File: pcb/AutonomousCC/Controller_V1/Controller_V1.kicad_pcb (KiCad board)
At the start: 2 copper layers, 142.9 x 87.6 mm, 18 parts, among them J1 Antenna_Conn_02x04_Odd_Even, J2 USB1130-15-A_REVA, SW1 SW_12mm_Push, SW2 SW_12mm_Push, U1 COM-09032, U2 Pico, U3 COM-09032

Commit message: Updated Tracing
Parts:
- turned VR1 to 270 degrees
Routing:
- net +3V3: track 0.00 -> 216.9 mm, vias 0 -> 2
- net +5V: track 0.00 -> 168.5 mm
- net GP04: track 0.00 -> 71.6 mm, vias 0 -> 1
- net GP27: track 0.00 -> 71.1 mm
- net GP28: track 0.00 -> 65.6 mm
- net GP06: track 0.00 -> 58.8 mm, vias 0 -> 1
- net GP26: track 0.00 -> 52.3 mm
- net GP07: track 0.00 -> 51.4 mm, vias 0 -> 1
- net GP15: track 0.00 -> 41.3 mm
- net GP10: track 0.00 -> 39.2 mm
- net GP16: track 0.00 -> 37.1 mm
- net GP09: track 0.00 -> 32.9 mm
- net GP14: track 0.00 -> 28.6 mm
- net Net-(D1-Pad2): track 0.00 -> 25.2 mm
- net GP17: track 0.00 -> 25.2 mm
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
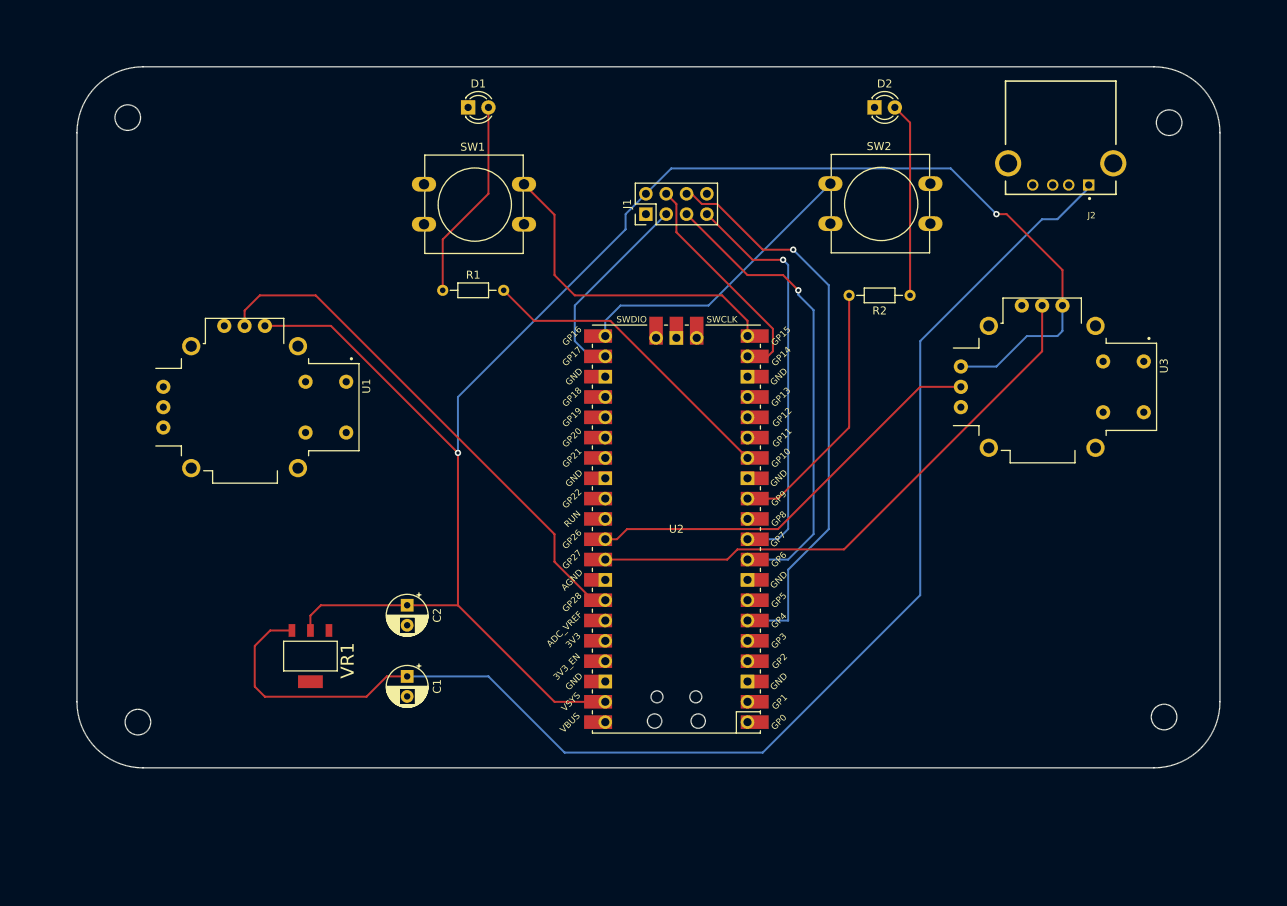
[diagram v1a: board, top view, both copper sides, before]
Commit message: Updated Ground Layer
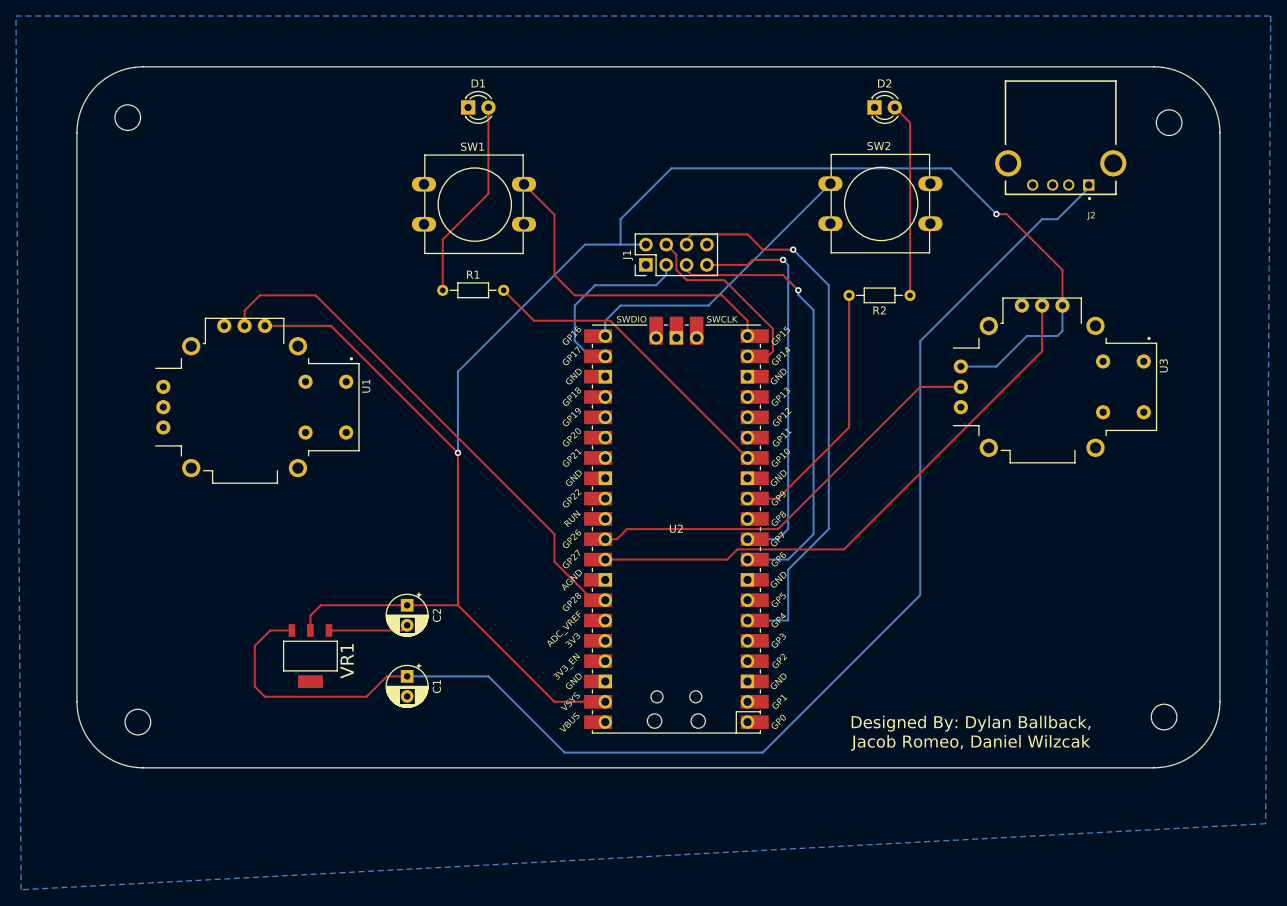
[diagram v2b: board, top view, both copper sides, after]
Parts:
- moved J1 6.35 mm to (170.8, 75.6)
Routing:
- net GND: track 0.00 -> 10.0 mm
- net +3V3: track 216.9 -> 224.0 mm
- net GP14: track 28.6 -> 25.1 mm
- net GP06: track 58.8 -> 56.5 mm
- net GP07: track 51.4 -> 49.3 mm
- net GP17: track 25.2 -> 23.3 mm
- net GP04: track 71.6 -> 70.4 mm
- added copper zone on B.Cu, net GND
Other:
- board text added: "Designed By: Dylan Ballback, Jacob Romeo, Daniel Wilzcak"
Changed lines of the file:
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@@
   (general
     (thickness 1.6)
-    (drawings 8)
-    (tracks 122)
+    (drawings 9)
+    (tracks 133)
     (zones 0)
     (modules 18)
@@
   )
   (module Connector_PinHeader_2.54mm:PinHeader_2x04_P2.54mm_Vertical (layer F.Cu)
-    (at 170.815 69.215 90)
+    (at 170.815 75.565 90)
     (descr "Through hole straight pin header, 2x04, 2.54mm pitch, double rows")
     (tags "Through hole pin header THT 2x04 2.54mm double row")
@@
     )
   )
+  (gr_text "Designed By: Dylan Ballback, \nJacob Romeo, Daniel Wilzcak\n" (at 211.455 133.985) (layer F.SilkS)
+    (effects (font (size 1.5 1.5) (thickness 0.25)))
+  )
   (gr_arc (start 234.315 59.055) (end 242.57 59.055) (angle -90) (layer Edge.Cuts) (width 0.05))
   (gr_arc (start 107.95 59.055) (end 107.95 50.8) (angle -90) (layer Edge.Cuts) (width 0.05))
@@
   (segment (start 187.96 74.93) (end 187.96 74.93) (width 0.25) (layer B.Cu) (net 2))
   (via (at 187.96 74.93) (size 0.8) (drill 0.4) (layers F.Cu B.Cu) (net 2))
-  (segment (start 184.15 74.93) (end 178.435 69.215) (width 0.25) (layer F.Cu) (net 2))
+  (segment (start 183.515 75.565) (end 178.435 75.565) (width 0.25) (layer F.Cu) (net 2))
+  (segment (start 184.15 74.93) (end 183.515 75.565) (width 0.25) (layer F.Cu) (net 2))
   (segment (start 187.96 74.93) (end 184.15 74.93) (width 0.25) (layer F.Cu) (net 2))
   (segment (start 183.515 120.015) (end 188.595 120.015) (width 0.25) (layer B.Cu) (net 3))
@@
   (segment (start 189.23 73.66) (end 189.23 73.66) (width 0.25) (layer B.Cu) (net 3))
   (via (at 189.23 73.66) (size 0.8) (drill 0.4) (layers F.Cu B.Cu) (net 3))
-  (segment (start 176.53 66.675) (end 175.895 66.675) (width 0.25) (layer F.Cu) (net 3))
-  (segment (start 177.8 67.945) (end 176.53 66.675) (width 0.25) (layer F.Cu) (net 3))
-  (segment (start 179.705 67.945) (end 177.8 67.945) (width 0.25) (layer F.Cu) (net 3))
-  (segment (start 185.42 73.66) (end 179.705 67.945) (width 0.25) (layer F.Cu) (net 3))
+  (segment (start 176.53 71.755) (end 175.895 72.39) (width 0.25) (layer F.Cu) (net 3))
+  (segment (start 183.515 71.755) (end 176.53 71.755) (width 0.25) (layer F.Cu) (net 3))
+  (segment (start 185.42 73.66) (end 183.515 71.755) (width 0.25) (layer F.Cu) (net 3))
+  (segment (start 175.895 72.39) (end 175.895 73.025) (width 0.25) (layer F.Cu) (net 3))
   (segment (start 189.23 73.66) (end 185.42 73.66) (width 0.25) (layer F.Cu) (net 3))
   (via (at 189.86501 78.74) (size 0.8) (drill 0.4) (layers F.Cu B.Cu) (net 4))
-  (segment (start 189.865 78.74) (end 189.86501 78.74) (width 0.25) (layer F.Cu) (net 4))
-  (segment (start 187.96 76.835) (end 189.865 78.74) (width 0.25) (layer F.Cu) (net 4))
-  (segment (start 183.515 76.835) (end 187.96 76.835) (width 0.25) (layer F.Cu) (net 4))
-  (segment (start 175.895 69.215) (end 183.515 76.835) (width 0.25) (layer F.Cu) (net 4))
   (segment (start 189.86501 79.305685) (end 189.86501 78.74) (width 0.25) (layer B.Cu) (net 4))
   (segment (start 188.595 112.395) (end 191.77 109.22) (width 0.25) (layer B.Cu) (net 4))
@@
   (segment (start 191.77 109.22) (end 191.77 81.210675) (width 0.25) (layer B.Cu) (net 4))
   (segment (start 183.515 112.395) (end 188.595 112.395) (width 0.25) (layer B.Cu) (net 4))
+  (segment (start 187.96 76.835) (end 189.865 78.74) (width 0.25) (layer F.Cu) (net 4))
+  (segment (start 176.53 76.835) (end 187.96 76.835) (width 0.25) (layer F.Cu) (net 4))
+  (segment (start 189.865 78.74) (end 189.86501 78.74) (width 0.25) (layer F.Cu) (net 4))
+  (segment (start 175.895 76.2) (end 176.53 76.835) (width 0.25) (layer F.Cu) (net 4))
+  (segment (start 175.895 75.565) (end 175.895 76.2) (width 0.25) (layer F.Cu) (net 4))
+  (segment (start 174.625 76.201411) (end 174.625 74.295) (width 0.25) (layer F.Cu) (net 5))
   (segment (start 183.515 86.995) (end 186.055 86.995) (width 0.25) (layer F.Cu) (net 5))
   (segment (start 186.055 86.995) (end 186.69 86.36) (width 0.25) (layer F.Cu) (net 5))
-  (segment (start 186.69 83.544998) (end 174.625 71.479998) (width 0.25) (layer F.Cu) (net 5))
+  (segment (start 180.615002 77.47) (end 175.893589 77.47) (width 0.25) (layer F.Cu) (net 5))
   (segment (start 186.69 86.36) (end 186.69 83.544998) (width 0.25) (layer F.Cu) (net 5))
-  (segment (start 174.625 71.479998) (end 174.625 67.945) (width 0.25) (layer F.Cu) (net 5))
-  (segment (start 174.625 67.945) (end 173.355 66.675) (width 0.25) (layer F.Cu) (net 5))
+  (segment (start 186.69 83.544998) (end 180.615002 77.47) (width 0.25) (layer F.Cu) (net 5))
+  (segment (start 175.893589 77.47) (end 174.625 76.201411) (width 0.25) (layer F.Cu) (net 5))
+  (segment (start 174.625 74.295) (end 173.355 73.025) (width 0.25) (layer F.Cu) (net 5))
+  (segment (start 164.465 78.105) (end 172.085 78.105) (width 0.25) (layer B.Cu) (net 6))
+  (segment (start 161.925 80.645) (end 164.465 78.105) (width 0.25) (layer B.Cu) (net 6))
+  (segment (start 161.925 85.09) (end 161.925 80.645) (width 0.25) (layer B.Cu) (net 6))
+  (segment (start 163.83 86.995) (end 161.925 85.09) (width 0.25) (layer B.Cu) (net 6))
   (segment (start 165.735 86.995) (end 163.83 86.995) (width 0.25) (layer B.Cu) (net 6))
-  (segment (start 163.83 86.995) (end 161.925 85.09) (width 0.25) (layer B.Cu) (net 6))
-  (segment (start 161.925 80.645) (end 173.355 69.215) (width 0.25) (layer B.Cu) (net 6))
-  (segment (start 161.925 85.09) (end 161.925 80.645) (width 0.25) (layer B.Cu) (net 6))
+  (segment (start 173.355 75.565) (end 173.355 76.835) (width 0.25) (layer B.Cu) (net 6))
+  (segment (start 173.355 76.835) (end 172.085 78.105) (width 0.25) (layer B.Cu) (net 6))
   (segment (start 128.8796 121.2596) (end 128.8796 119.4054) (width 0.25) (layer F.Cu) (net 7))
   (segment (start 130.175 118.11) (end 140.97 118.11) (width 0.25) (layer F.Cu) (net 7))
@@
   (segment (start 147.32 99.06) (end 147.32 99.06) (width 0.25) (layer F.Cu) (net 7))
   (via (at 147.32 99.06) (size 0.8) (drill 0.4) (layers F.Cu B.Cu) (net 7))
-  (segment (start 170.815 66.675) (end 168.275 69.215) (width 0.25) (layer B.Cu) (net 7))
-  (segment (start 168.275 69.215) (end 168.275 71.12) (width 0.25) (layer B.Cu) (net 7))
-  (segment (start 147.32 92.075) (end 147.32 99.06) (width 0.25) (layer B.Cu) (net 7))
-  (segment (start 168.275 71.12) (end 147.32 92.075) (width 0.25) (layer B.Cu) (net 7))
-  (segment (start 170.815 66.675) (end 173.99 63.5) (width 0.25) (layer B.Cu) (net 7))
-  (segment (start 173.99 63.5) (end 208.915 63.5) (width 0.25) (layer B.Cu) (net 7))
-  (segment (start 208.915 63.5) (end 214.63 69.215) (width 0.25) (layer B.Cu) (net 7))
   (segment (start 214.63 69.215) (end 214.63 69.215) (width 0.25) (layer B.Cu) (net 7))
   (via (at 214.63 69.215) (size 0.8) (drill 0.4) (layers F.Cu B.Cu) (net 7))
@@
   (segment (start 222.885 83.82) (end 222.25 84.455) (width 0.25) (layer B.Cu) (net 7))
   (segment (start 222.885 80.645) (end 222.885 83.82) (width 0.25) (layer B.Cu) (net 7))
+  (segment (start 147.32 92.075) (end 147.32 99.06) (width 0.25) (layer B.Cu) (net 7))
+  (segment (start 167.64 73.025) (end 170.815 73.025) (width 0.25) (layer B.Cu) (net 7))
+  (segment (start 208.915 63.5) (end 214.63 69.215) (width 0.25) (layer B.Cu) (net 7))
+  (segment (start 173.99 63.5) (end 208.915 63.5) (width 0.25) (layer B.Cu) (net 7))
+  (segment (start 167.64 69.85) (end 173.99 63.5) (width 0.25) (layer B.Cu) (net 7))
+  (segment (start 167.64 73.025) (end 167.64 69.85) (width 0.25) (layer B.Cu) (net 7))
+  (segment (start 147.32 88.9) (end 147.32 93.345) (width 0.25) (layer B.Cu) (net 7))
+  (segment (start 163.195 73.025) (end 147.32 88.9) (width 0.25) (layer B.Cu) (net 7))
+  (segment (start 167.64 73.025) (end 163.195 73.025) (width 0.25) (layer B.Cu) (net 7))
+  (segment (start 140.3204 121.2596) (end 140.97 120.61) (width 0.25) (layer F.Cu) (net 8))
+  (segment (start 131.191 121.2596) (end 140.3204 121.2596) (width 0.25) (layer F.Cu) (net 8))
   (segment (start 164.189998 117.475) (end 165.735 117.475) (width 0.25) (layer F.Cu) (net 9))
   (segment (start 129.54 79.375) (end 159.385 109.22) (width 0.25) (layer F.Cu) (net 9))
@@
   (segment (start 203.835 57.785) (end 201.93 55.88) (width 0.25) (layer F.Cu) (net 59))
   (segment (start 203.835 79.375) (end 203.835 57.785) (width 0.25) (layer F.Cu) (net 59))
+  (zone (net 8) (net_name GND) (layer B.Cu) (hatch edge 0.508)
+    (connect_pads (clearance 0.508))
+    (min_thickness 0.254)
+    (fill yes (arc_segments 32) (thermal_gap 0.508) (thermal_bridge_width 0.508))
+    (polygon
+      (pts
+        (xy 248.285 145.415) (xy 92.71 153.67) (xy 92.075 44.45) (xy 248.92 44.45)
+      )
+    )
+  )
 )

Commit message: Update Silk Mask
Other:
- board text added: "Controller V1"
- board text added: "EPPL"
- board text added: "Engineering Physics Propulsion Lab"
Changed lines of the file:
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@@
   (general
     (thickness 1.6)
-    (drawings 9)
+    (drawings 12)
     (tracks 133)
     (zones 0)
@@
     )
   )
+  (gr_text "Controller V1\n" (at 119.38 54.61) (layer F.SilkS)
+    (effects (font (size 1.5 1.5) (thickness 0.3)))
+  )
+  (gr_text "Engineering Physics Propulsion Lab" (at 217.17 126.365) (layer F.SilkS)
+    (effects (font (size 1.5 1.5) (thickness 0.3)))
+  )
+  (gr_text EPPL (at 217.805 118.745) (layer F.SilkS)
+    (effects (font (size 8 8) (thickness 2)))
+  )
   (gr_text "Designed By: Dylan Ballback, \nJacob Romeo, Daniel Wilzcak\n" (at 211.455 133.985) (layer F.SilkS)
